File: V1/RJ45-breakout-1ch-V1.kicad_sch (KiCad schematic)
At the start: 2 parts, among them J1 RJ45, J2 Screw_Terminal_01x04

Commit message: Footprint updated
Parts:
- removed J2: Screw_Terminal_01x04, Tales:TerminalBlock_Phoenix_MKDS-3-4-5.08_1x04_P5.08mm_Horizontal, symbol Connector:Screw_Terminal_01x04
- added J2: SWITCHES, symbol Connector_Generic:Conn_01x04
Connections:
- net at J1.1, J1.2: now also J2.1 (Pin_1)
- net at J1.3, J1.6: now also J2.2 (Pin_2)
- net at J1.4, J1.5: now also J2.3 (Pin_3)
- net at J1.7, J1.8: now also J2.4 (Pin_4)
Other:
- note added: "J2 PIN 1 - 24V J2 PIN 2 - SWITCH 1 J2 PIN 3 - SWITCH 2 J2 PIN 4 - SWITCH 3"
- note added: "OPÇÕES RJ45 AMPHENOL RJE08-188-0110 MOUSER 523-RJE081880110 VERTICAL AMPHENOL RJHSE5080 MOUSER 523-RJHSE-5080 HORIZONTAL MOLEX 424108312 JLCPCB C114100 VERTICAL CKMTW R-RJ45R08P-A802 JLCPCB C508567 45º TE CONNECTIVITY 5569284-1 JLCPCB C305935 VERTICAL"
- moved on the sheet: J1
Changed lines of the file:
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@@
     (rev "V1")
   )
-  (junction (at 146.05 99.06) (diameter 0) (color 0 0 0 0)
+  (junction (at 152.4 99.06) (diameter 0) (color 0 0 0 0)
   )
-  (junction (at 140.97 109.22) (diameter 0) (color 0 0 0 0)
+  (junction (at 147.32 109.22) (diameter 0) (color 0 0 0 0)
   )
-  (junction (at 140.97 93.98) (diameter 0) (color 0 0 0 0)
+  (junction (at 147.32 93.98) (diameter 0) (color 0 0 0 0)
   )
-  (junction (at 140.97 101.6) (diameter 0) (color 0 0 0 0)
+  (junction (at 147.32 101.6) (diameter 0) (color 0 0 0 0)
   )
-  (wire (pts (xy 140.97 96.52) (xy 140.97 93.98))
+  (wire (pts (xy 147.32 96.52) (xy 147.32 93.98))
     (stroke (width 0) (type default))
   )
-  (wire (pts (xy 137.16 104.14) (xy 140.97 104.14))
+  (wire (pts (xy 143.51 104.14) (xy 147.32 104.14))
     (stroke (width 0) (type default))
   )
-  (wire (pts (xy 154.94 101.6) (xy 157.48 101.6))
+  (wire (pts (xy 161.29 101.6) (xy 163.83 101.6))
     (stroke (width 0) (type default))
   )
-  (wire (pts (xy 140.97 93.98) (xy 137.16 93.98))
+  (wire (pts (xy 147.32 93.98) (xy 143.51 93.98))
     (stroke (width 0) (type default))
   )
-  (wire (pts (xy 140.97 111.76) (xy 140.97 109.22))
+  (wire (pts (xy 147.32 111.76) (xy 147.32 109.22))
     (stroke (width 0) (type default))
   )
-  (wire (pts (xy 152.4 101.6) (xy 152.4 96.52))
+  (wire (pts (xy 158.75 101.6) (xy 158.75 96.52))
     (stroke (width 0) (type default))
   )
-  (wire (pts (xy 137.16 96.52) (xy 140.97 96.52))
+  (wire (pts (xy 143.51 96.52) (xy 147.32 96.52))
     (stroke (width 0) (type default))
   )
-  (wire (pts (xy 140.97 101.6) (xy 137.16 101.6))
+  (wire (pts (xy 147.32 101.6) (xy 143.51 101.6))
     (stroke (width 0) (type default))
   )
-  (wire (pts (xy 140.97 109.22) (xy 137.16 109.22))
+  (wire (pts (xy 147.32 109.22) (xy 143.51 109.22))
     (stroke (width 0) (type default))
   )
-  (wire (pts (xy 146.05 99.06) (xy 137.16 99.06))
+  (wire (pts (xy 152.4 99.06) (xy 143.51 99.06))
     (stroke (width 0) (type default))
   )
-  (wire (pts (xy 146.05 99.06) (xy 157.48 99.06))
+  (wire (pts (xy 152.4 99.06) (xy 163.83 99.06))
     (stroke (width 0) (type default))
   )
-  (wire (pts (xy 140.97 101.6) (xy 152.4 101.6))
+  (wire (pts (xy 147.32 101.6) (xy 158.75 101.6))
     (stroke (width 0) (type default))
   )
-  (wire (pts (xy 146.05 106.68) (xy 146.05 99.06))
+  (wire (pts (xy 152.4 106.68) (xy 152.4 99.06))
     (stroke (width 0) (type default))
   )
-  (wire (pts (xy 140.97 93.98) (xy 157.48 93.98))
+  (wire (pts (xy 147.32 93.98) (xy 163.83 93.98))
     (stroke (width 0) (type default))
   )
-  (wire (pts (xy 137.16 106.68) (xy 146.05 106.68))
+  (wire (pts (xy 143.51 106.68) (xy 152.4 106.68))
     (stroke (width 0) (type default))
   )
-  (wire (pts (xy 154.94 109.22) (xy 154.94 101.6))
+  (wire (pts (xy 161.29 109.22) (xy 161.29 101.6))
     (stroke (width 0) (type default))
   )
-  (wire (pts (xy 137.16 111.76) (xy 140.97 111.76))
+  (wire (pts (xy 143.51 111.76) (xy 147.32 111.76))
     (stroke (width 0) (type default))
   )
-  (wire (pts (xy 140.97 104.14) (xy 140.97 101.6))
+  (wire (pts (xy 147.32 104.14) (xy 147.32 101.6))
     (stroke (width 0) (type default))
   )
-  (wire (pts (xy 152.4 96.52) (xy 157.48 96.52))
+  (wire (pts (xy 158.75 96.52) (xy 163.83 96.52))
     (stroke (width 0) (type default))
   )
-  (wire (pts (xy 140.97 109.22) (xy 154.94 109.22))
+  (wire (pts (xy 147.32 109.22) (xy 161.29 109.22))
     (stroke (width 0) (type default))
   )
-  (symbol (lib_id "Connector:Screw_Terminal_01x04") (at 162.56 99.06 0) (mirror x) (unit 1)
+  (text "OPÇÕES RJ45\n\nAMPHENOL RJE08-188-0110\nMOUSER 523-RJE081880110\nVERTICAL\n\nAMPHENOL RJHSE5080\nMOUSER 523-RJHSE-5080\nHORIZONTAL\n\nMOLEX 424108312\nJLCPCB C114100\nVERTICAL\n\nCKMTW R-RJ45R08P-A802\nJLCPCB C508567\n45º\n\nTE CONNECTIVITY 5569284-1\nJLCPCB C305935\nVERTICAL"
+    (at 83.82 121.92 0)
+    (effects (font (size 1.27 1.27)) (justify left bottom))
+  )
+  (text "J2 PIN 1 - 24V\nJ2 PIN 2 - SWITCH 1\nJ2 PIN 3 - SWITCH 2\nJ2 PIN 4 - SWITCH 3"
+    (at 171.45 114.3 0)
+    (effects (font (size 1.27 1.27)) (justify left bottom))
+  )
+  (symbol (lib_id "Connector:RJ45") (at 133.35 104.14 0) (unit 1)
     (in_bom yes) (on_board yes) (dnp no)
-    (property "Reference" "J2" (at 166.37 99.06 0)
+    (property "Reference" "J1" (at 134.7978 87.1982 0)
       (effects (font (size 1.27 1.27)))
     )
-    (property "Value" "Screw_Terminal_01x04" (at 175.26 96.52 0)
+    (property "Value" "RJ45" (at 134.7978 89.5096 0)
       (effects (font (size 1.27 1.27)))
     )
-    (property "Footprint" "Tales:TerminalBlock_Phoenix_MKDS-3-4-5.08_1x04_P5.08mm_Horizontal" (at 162.56 99.06 0)
+    (property "Footprint" "Tales:RJ45_Amphenol_RJHSE5080" (at 133.35 103.505 90)
       (effects (font (size 1.27 1.27)) hide)
     )
-    (property "Datasheet" "~" (at 162.56 99.06 0)
+    (property "Datasheet" "~" (at 133.35 103.505 90)
       (effects (font (size 1.27 1.27)) hide)
     )
-    (property "Case" "~" (at 162.56 99.06 0)
+    (property "Case" "~" (at 133.35 104.14 0)
       (effects (font (size 1.27 1.27)) hide)
     )
-    (property "Mfr" "Metaltex" (at 162.56 99.06 0)
+    (property "Mfr" "Amphenol" (at 133.35 104.14 0)
       (effects (font (size 1.27 1.27)) hide)
     )
-    (property "Mfr PN" "2x BR902V" (at 162.56 99.06 0)
+    (property "Mfr PN" "RJHSE-5080" (at 133.35 104.14 0)
       (effects (font (size 1.27 1.27)) hide)
     )
-    (property "Vendor" "Eletropecas" (at 162.56 99.06 0)
+    (property "Vendor" "Mouser" (at 133.35 104.14 0)
       (effects (font (size 1.27 1.27)) hide)
     )
-    (property "Vendor PN" "2x 29273" (at 162.56 99.06 0)
+    (property "Vendor PN" "523-RJHSE-5080" (at 133.35 104.14 0)
       (effects (font (size 1.27 1.27)) hide)
     )
-    (property "JLCPCB BOM" "~" (at 162.56 99.06 0)
+    (property "JLCPCB BOM" "~" (at 133.35 104.14 0)
       (effects (font (size 1.27 1.27)) hide)
     )
-    (property "LCSC Part" "~" (at 162.56 99.06 0)
-      (effects (font (size 1.27 1.27)) hide)
-    )
-    (pin "1")
-    (pin "2")
-    (pin "3")
-    (pin "4")
-    (instances
-      (project "RJ45-breakout-1ch-V1"
-        (path "/78f88cf6-751c-4e9b-ae75-fb8b6d44ff39"
-          (reference "J2") (unit 1)
-        )
-      )
-    )
-  )
-  (symbol (lib_id "Connector:RJ45") (at 127 104.14 0) (unit 1)
-    (in_bom yes) (on_board yes) (dnp no)
-    (property "Reference" "J1" (at 128.4478 87.1982 0)
-      (effects (font (size 1.27 1.27)))
-    )
-    (property "Value" "RJ45" (at 128.4478 89.5096 0)
-      (effects (font (size 1.27 1.27)))
-    )
-    (property "Footprint" "Tales:RJ45_Amphenol_RJHSE5080" (at 127 103.505 90)
-      (effects (font (size 1.27 1.27)) hide)
-    )
-    (property "Datasheet" "~" (at 127 103.505 90)
-      (effects (font (size 1.27 1.27)) hide)
-    )
-    (property "Case" "~" (at 127 104.14 0)
-      (effects (font (size 1.27 1.27)) hide)
-    )
-    (property "Mfr" "Amphenol" (at 127 104.14 0)
-      (effects (font (size 1.27 1.27)) hide)
-    )
-    (property "Mfr PN" "RJHSE-5080" (at 127 104.14 0)
-      (effects (font (size 1.27 1.27)) hide)
-    )
-    (property "Vendor" "Mouser" (at 127 104.14 0)
-      (effects (font (size 1.27 1.27)) hide)
-    )
-    (property "Vendor PN" "523-RJHSE-5080" (at 127 104.14 0)
-      (effects (font (size 1.27 1.27)) hide)
-    )
-    (property "JLCPCB BOM" "~" (at 127 104.14 0)
-      (effects (font (size 1.27 1.27)) hide)
-    )
-    (property "LCSC Part" "~" (at 127 104.14 0)
+    (property "LCSC Part" "~" (at 133.35 104.14 0)
       (effects (font (size 1.27 1.27)) hide)
     )
@@
         )
       )
+    )
+  )
+  (symbol (lib_id "Connector_Generic:Conn_01x04") (at 168.91 99.06 0) (mirror x) (unit 1)
+    (in_bom yes) (on_board yes) (dnp no)
+    (property "Reference" "J2" (at 171.45 98.425 0)
+      (effects (font (size 1.27 1.27)) (justify left))
+    )
+    (property "Value" "SWITCHES" (at 171.45 95.885 0)
+      (effects (font (size 1.27 1.27)) (justify left))
+    )
+    (property "Footprint" "" (at 168.91 99.06 0)
+      (effects (font (size 1.27 1.27)) hide)
+    )
+    (property "Datasheet" "~" (at 168.91 99.06 0)
+      (effects (font (size 1.27 1.27)) hide)
+    )
+    (pin "1")
+    (pin "2")
+    (pin "3")
+    (pin "4")
+    (instances
+      (project "RJ45-breakout-1ch-V1"
+        (path "/78f88cf6-751c-4e9b-ae75-fb8b6d44ff39"
+          (reference "J2") (unit 1)
+        )
+      )

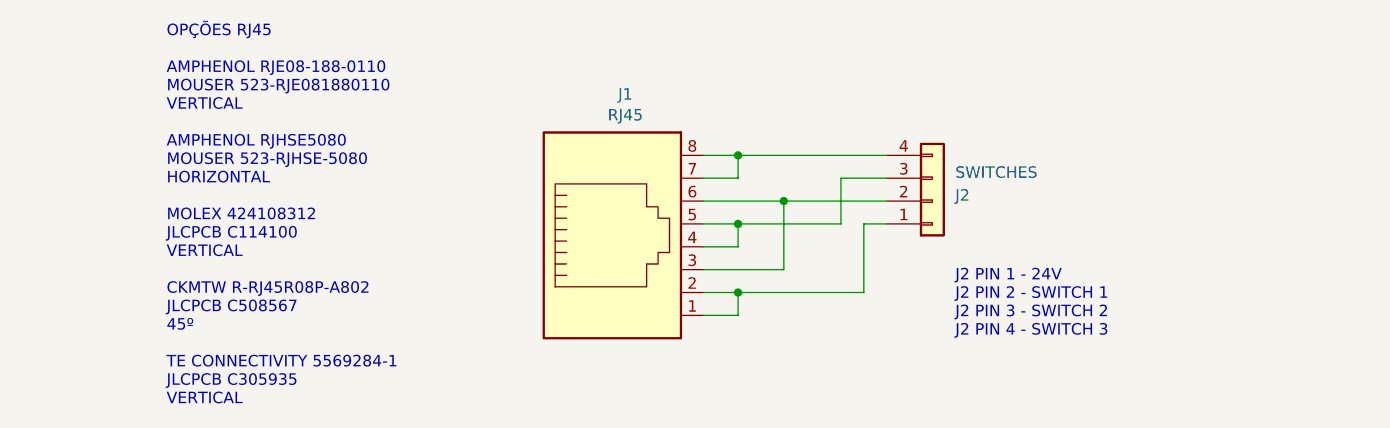
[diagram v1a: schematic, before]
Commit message: PCB size optimization
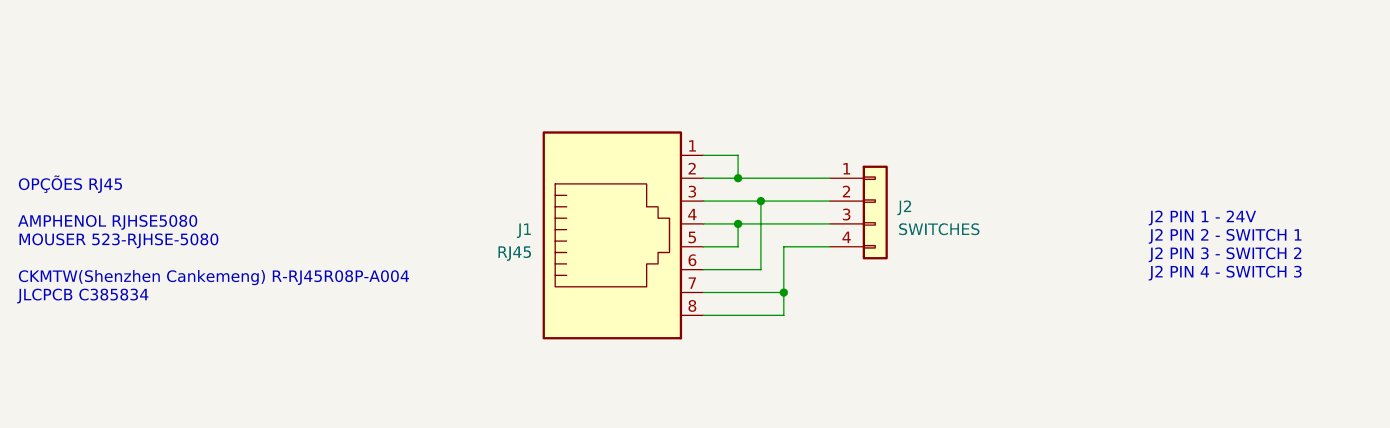
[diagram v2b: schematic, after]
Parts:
- J1: JLCPCB BOM (none) -> 1; LCSC Part (none) -> C385834; Mfr Amphenol -> Ckmtw(Shenzhen Cankemeng); Mfr PN RJHSE-5080 -> R-RJ45R08P-A004; Vendor Mouser -> JLCPCB; Vendor PN 523-RJHSE-5080 -> C385834
- J2: footprint (none) -> Tales:TerminalBlock_Phoenix_MKDS-3-4-5.08_1x04_P5.08mm_Horizontal; JLCPCB BOM (none) -> 1; LCSC Part (none) -> C2915641; Mfr (none) -> DIBO; Mfr PN (none) -> DB128V-5.08-4P-GN-S; Vendor (none) -> JLCPCB; Vendor PN (none) -> C2915641
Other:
- note added: "OPÇÕES RJ45 AMPHENOL RJHSE5080 MOUSER 523-RJHSE-5080 CKMTW(Shenzhen Cankemeng) R-RJ45R08P-A004 JLCPCB C385834"
- note removed: "OPÇÕES RJ45 AMPHENOL RJE08-188-0110 MOUSER 523-RJE081880110 VERTICAL AMPHENOL RJHSE5080 MOUSER 523-RJHSE-5080 HORIZONTAL MOLEX 424108312 JLCPCB C114100 VERTICAL CKMTW R-RJ45R08P-A802 JLCPCB C508567 45º TE CONNECTIVITY 5569284-1 JLCPCB C305935 VERTICAL"
- moved on the sheet: J2
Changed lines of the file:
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@@
     (rev "V1")
   )
-  (junction (at 152.4 99.06) (diameter 0) (color 0 0 0 0)
+  (junction (at 147.32 96.52) (diameter 0) (color 0 0 0 0)
   )
-  (junction (at 147.32 109.22) (diameter 0) (color 0 0 0 0)
+  (junction (at 149.86 99.06) (diameter 0) (color 0 0 0 0)
   )
-  (junction (at 147.32 93.98) (diameter 0) (color 0 0 0 0)
+  (junction (at 152.4 109.22) (diameter 0) (color 0 0 0 0)
   )
   (junction (at 147.32 101.6) (diameter 0) (color 0 0 0 0)
@@
     (stroke (width 0) (type default))
   )
+  (wire (pts (xy 149.86 99.06) (xy 157.48 99.06))
+    (stroke (width 0) (type default))
+  )
   (wire (pts (xy 143.51 104.14) (xy 147.32 104.14))
     (stroke (width 0) (type default))
   )
-  (wire (pts (xy 161.29 101.6) (xy 163.83 101.6))
+  (wire (pts (xy 152.4 104.14) (xy 157.48 104.14))
     (stroke (width 0) (type default))
   )
@@
     (stroke (width 0) (type default))
   )
-  (wire (pts (xy 147.32 111.76) (xy 147.32 109.22))
-    (stroke (width 0) (type default))
-  )
-  (wire (pts (xy 158.75 101.6) (xy 158.75 96.52))
+  (wire (pts (xy 152.4 111.76) (xy 152.4 109.22))
     (stroke (width 0) (type default))
   )
@@
     (stroke (width 0) (type default))
   )
-  (wire (pts (xy 147.32 109.22) (xy 143.51 109.22))
+  (wire (pts (xy 147.32 101.6) (xy 157.48 101.6))
     (stroke (width 0) (type default))
   )
-  (wire (pts (xy 152.4 99.06) (xy 143.51 99.06))
+  (wire (pts (xy 149.86 99.06) (xy 143.51 99.06))
     (stroke (width 0) (type default))
   )
-  (wire (pts (xy 152.4 99.06) (xy 163.83 99.06))
+  (wire (pts (xy 149.86 106.68) (xy 149.86 99.06))
     (stroke (width 0) (type default))
   )
-  (wire (pts (xy 147.32 101.6) (xy 158.75 101.6))
+  (wire (pts (xy 147.32 96.52) (xy 157.48 96.52))
     (stroke (width 0) (type default))
   )
-  (wire (pts (xy 152.4 106.68) (xy 152.4 99.06))
+  (wire (pts (xy 143.51 106.68) (xy 149.86 106.68))
     (stroke (width 0) (type default))
   )
-  (wire (pts (xy 147.32 93.98) (xy 163.83 93.98))
+  (wire (pts (xy 152.4 109.22) (xy 152.4 104.14))
     (stroke (width 0) (type default))
   )
-  (wire (pts (xy 143.51 106.68) (xy 152.4 106.68))
-    (stroke (width 0) (type default))
-  )
-  (wire (pts (xy 161.29 109.22) (xy 161.29 101.6))
-    (stroke (width 0) (type default))
-  )
-  (wire (pts (xy 143.51 111.76) (xy 147.32 111.76))
+  (wire (pts (xy 143.51 111.76) (xy 152.4 111.76))
     (stroke (width 0) (type default))
   )
@@
     (stroke (width 0) (type default))
   )
-  (wire (pts (xy 158.75 96.52) (xy 163.83 96.52))
+  (wire (pts (xy 143.51 109.22) (xy 152.4 109.22))
     (stroke (width 0) (type default))
   )
-  (wire (pts (xy 147.32 109.22) (xy 161.29 109.22))
-    (stroke (width 0) (type default))
-  )
-  (text "OPÇÕES RJ45\n\nAMPHENOL RJE08-188-0110\nMOUSER 523-RJE081880110\nVERTICAL\n\nAMPHENOL RJHSE5080\nMOUSER 523-RJHSE-5080\nHORIZONTAL\n\nMOLEX 424108312\nJLCPCB C114100\nVERTICAL\n\nCKMTW R-RJ45R08P-A802\nJLCPCB C508567\n45º\n\nTE CONNECTIVITY 5569284-1\nJLCPCB C305935\nVERTICAL"
-    (at 83.82 121.92 0)
+  (text "OPÇÕES RJ45\n\nAMPHENOL RJHSE5080\nMOUSER 523-RJHSE-5080\n\nCKMTW(Shenzhen Cankemeng) R-RJ45R08P-A004\nJLCPCB C385834\n"
+    (at 67.31 110.49 0)
     (effects (font (size 1.27 1.27)) (justify left bottom))
   )
   (text "J2 PIN 1 - 24V\nJ2 PIN 2 - SWITCH 1\nJ2 PIN 3 - SWITCH 2\nJ2 PIN 4 - SWITCH 3"
-    (at 171.45 114.3 0)
+    (at 193.04 107.95 0)
     (effects (font (size 1.27 1.27)) (justify left bottom))
   )
-  (symbol (lib_id "Connector:RJ45") (at 133.35 104.14 0) (unit 1)
-    (in_bom yes) (on_board yes) (dnp no)
-    (property "Reference" "J1" (at 134.7978 87.1982 0)
-      (effects (font (size 1.27 1.27)))
+  (symbol (lib_id "Connector:RJ45") (at 133.35 101.6 0) (mirror x) (unit 1)
+    (in_bom yes) (on_board yes) (dnp no) (fields_autoplaced)
+    (property "Reference" "J1" (at 124.46 102.235 0)
+      (effects (font (size 1.27 1.27)) (justify right))
     )
-    (property "Value" "RJ45" (at 134.7978 89.5096 0)
-      (effects (font (size 1.27 1.27)))
+    (property "Value" "RJ45" (at 124.46 104.775 0)
+      (effects (font (size 1.27 1.27)) (justify right))
     )
-    (property "Footprint" "Tales:RJ45_Amphenol_RJHSE5080" (at 133.35 103.505 90)
+    (property "Footprint" "Tales:RJ45_Amphenol_RJHSE5080" (at 133.35 102.235 90)
       (effects (font (size 1.27 1.27)) hide)
     )
-    (property "Datasheet" "~" (at 133.35 103.505 90)
+    (property "Datasheet" "~" (at 133.35 102.235 90)
       (effects (font (size 1.27 1.27)) hide)
     )
-    (property "Case" "~" (at 133.35 104.14 0)
+    (property "Case" "~" (at 133.35 101.6 0)
       (effects (font (size 1.27 1.27)) hide)
     )
-    (property "Mfr" "Amphenol" (at 133.35 104.14 0)
+    (property "Mfr" "Ckmtw(Shenzhen Cankemeng)" (at 133.35 101.6 0)
       (effects (font (size 1.27 1.27)) hide)
     )
-    (property "Mfr PN" "RJHSE-5080" (at 133.35 104.14 0)
+    (property "Mfr PN" "R-RJ45R08P-A004" (at 133.35 101.6 0)
       (effects (font (size 1.27 1.27)) hide)
     )
-    (property "Vendor" "Mouser" (at 133.35 104.14 0)
+    (property "Vendor" "JLCPCB" (at 133.35 101.6 0)
       (effects (font (size 1.27 1.27)) hide)
     )
-    (property "Vendor PN" "523-RJHSE-5080" (at 133.35 104.14 0)
+    (property "Vendor PN" "C385834" (at 133.35 101.6 0)
       (effects (font (size 1.27 1.27)) hide)
     )
-    (property "JLCPCB BOM" "~" (at 133.35 104.14 0)
+    (property "JLCPCB BOM" "1" (at 133.35 101.6 0)
       (effects (font (size 1.27 1.27)) hide)
     )
-    (property "LCSC Part" "~" (at 133.35 104.14 0)
+    (property "LCSC Part" "C385834" (at 133.35 101.6 0)
       (effects (font (size 1.27 1.27)) hide)
     )
@@
     )
   )
-  (symbol (lib_id "Connector_Generic:Conn_01x04") (at 168.91 99.06 0) (mirror x) (unit 1)
-    (in_bom yes) (on_board yes) (dnp no)
-    (property "Reference" "J2" (at 171.45 98.425 0)
+  (symbol (lib_id "Connector_Generic:Conn_01x04") (at 162.56 99.06 0) (unit 1)
+    (in_bom yes) (on_board yes) (dnp no) (fields_autoplaced)
+    (property "Reference" "J2" (at 165.1 99.695 0)
       (effects (font (size 1.27 1.27)) (justify left))
     )
-    (property "Value" "SWITCHES" (at 171.45 95.885 0)
+    (property "Value" "SWITCHES" (at 165.1 102.235 0)
       (effects (font (size 1.27 1.27)) (justify left))
     )
-    (property "Footprint" "" (at 168.91 99.06 0)
+    (property "Footprint" "Tales:TerminalBlock_Phoenix_MKDS-3-4-5.08_1x04_P5.08mm_Horizontal" (at 162.56 99.06 0)
       (effects (font (size 1.27 1.27)) hide)
     )
-    (property "Datasheet" "~" (at 168.91 99.06 0)
+    (property "Datasheet" "~" (at 162.56 99.06 0)
       (effects (font (size 1.27 1.27)) hide)
     )
+    (property "Case" "~" (at 162.56 99.06 0)
+      (effects (font (size 1.27 1.27)) hide)
+    )
+    (property "JLCPCB BOM" "1" (at 162.56 99.06 0)
+      (effects (font (size 1.27 1.27)) hide)
+    )
+    (property "LCSC Part" "C2915641" (at 162.56 99.06 0)
+      (effects (font (size 1.27 1.27)) hide)
+    )
+    (property "Mfr" "DIBO" (at 162.56 99.06 0)
+      (effects (font (size 1.27 1.27)) hide)
+    )
+    (property "Mfr PN" "DB128V-5.08-4P-GN-S" (at 162.56 99.06 0)
+      (effects (font (size 1.27 1.27)) hide)
+    )
+    (property "Vendor" "JLCPCB" (at 162.56 99.06 0)
+      (effects (font (size 1.27 1.27)) hide)
+    )
+    (property "Vendor PN" "C2915641" (at 162.56 99.06 0)
+      (effects (font (size 1.27 1.27)) hide)
+    )

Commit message: Footprints updated
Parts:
- J1: footprint Tales:RJ45_Amphenol_RJHSE5080 -> Tales:RJ45_CKMTW_R-RJ45R08P-A004
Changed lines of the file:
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@@
       (effects (font (size 1.27 1.27)) (justify right))
     )
-    (property "Footprint" "Tales:RJ45_Amphenol_RJHSE5080" (at 133.35 102.235 90)
+    (property "Footprint" "Tales:RJ45_CKMTW_R-RJ45R08P-A004" (at 133.35 102.235 90)
       (effects (font (size 1.27 1.27)) hide)
     )

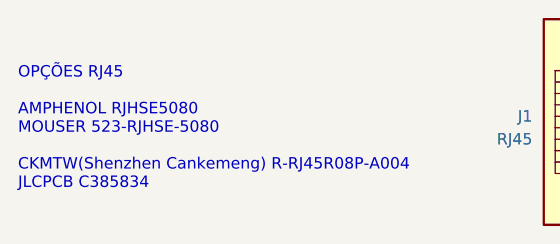
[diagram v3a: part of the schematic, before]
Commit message: Texts position adjusted
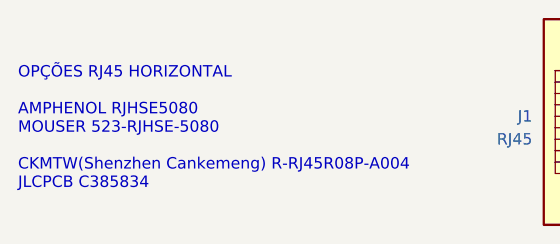
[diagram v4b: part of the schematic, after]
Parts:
- J2: footprint Tales:TerminalBlock_Phoenix_MKDS-3-4-5.08_1x04_P5.08mm_Horizontal -> Tales:TerminalBlock_Dibo_DB128L-5.08-4P_1x04_P5.08mm_Horizontal
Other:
- note added: "OPÇÕES RJ45 HORIZONTAL AMPHENOL RJHSE5080 MOUSER 523-RJHSE-5080 CKMTW(Shenzhen Cankemeng) R-RJ45R08P-A004 JLCPCB C385834"
- note removed: "OPÇÕES RJ45 AMPHENOL RJHSE5080 MOUSER 523-RJHSE-5080 CKMTW(Shenzhen Cankemeng) R-RJ45R08P-A004 JLCPCB C385834"
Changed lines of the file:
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@@
     (stroke (width 0) (type default))
   )
-  (text "OPÇÕES RJ45\n\nAMPHENOL RJHSE5080\nMOUSER 523-RJHSE-5080\n\nCKMTW(Shenzhen Cankemeng) R-RJ45R08P-A004\nJLCPCB C385834\n"
+  (text "OPÇÕES RJ45 HORIZONTAL\n\nAMPHENOL RJHSE5080\nMOUSER 523-RJHSE-5080\n\nCKMTW(Shenzhen Cankemeng) R-RJ45R08P-A004\nJLCPCB C385834\n"
     (at 67.31 110.49 0)
     (effects (font (size 1.27 1.27)) (justify left bottom))
@@
       (effects (font (size 1.27 1.27)) (justify left))
     )
-    (property "Footprint" "Tales:TerminalBlock_Phoenix_MKDS-3-4-5.08_1x04_P5.08mm_Horizontal" (at 162.56 99.06 0)
+    (property "Footprint" "Tales:TerminalBlock_Dibo_DB128L-5.08-4P_1x04_P5.08mm_Horizontal" (at 162.56 99.06 0)
       (effects (font (size 1.27 1.27)) hide)
     )
